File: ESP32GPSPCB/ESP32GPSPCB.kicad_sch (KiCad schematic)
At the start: 66 parts, among them J1 Conn_01x04_Socket, J2 USB_C_Receptacle_USB2.0_14P, J3 Conn_01x14_Socket, J4 Conn_01x04_Socket, J5 Boot Option, J6 Conn_01x04_Socket, J7 Conn_01x05_Socket, J8 Logic extra channel, SW1 SW_Push, U1 NEO-M8N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

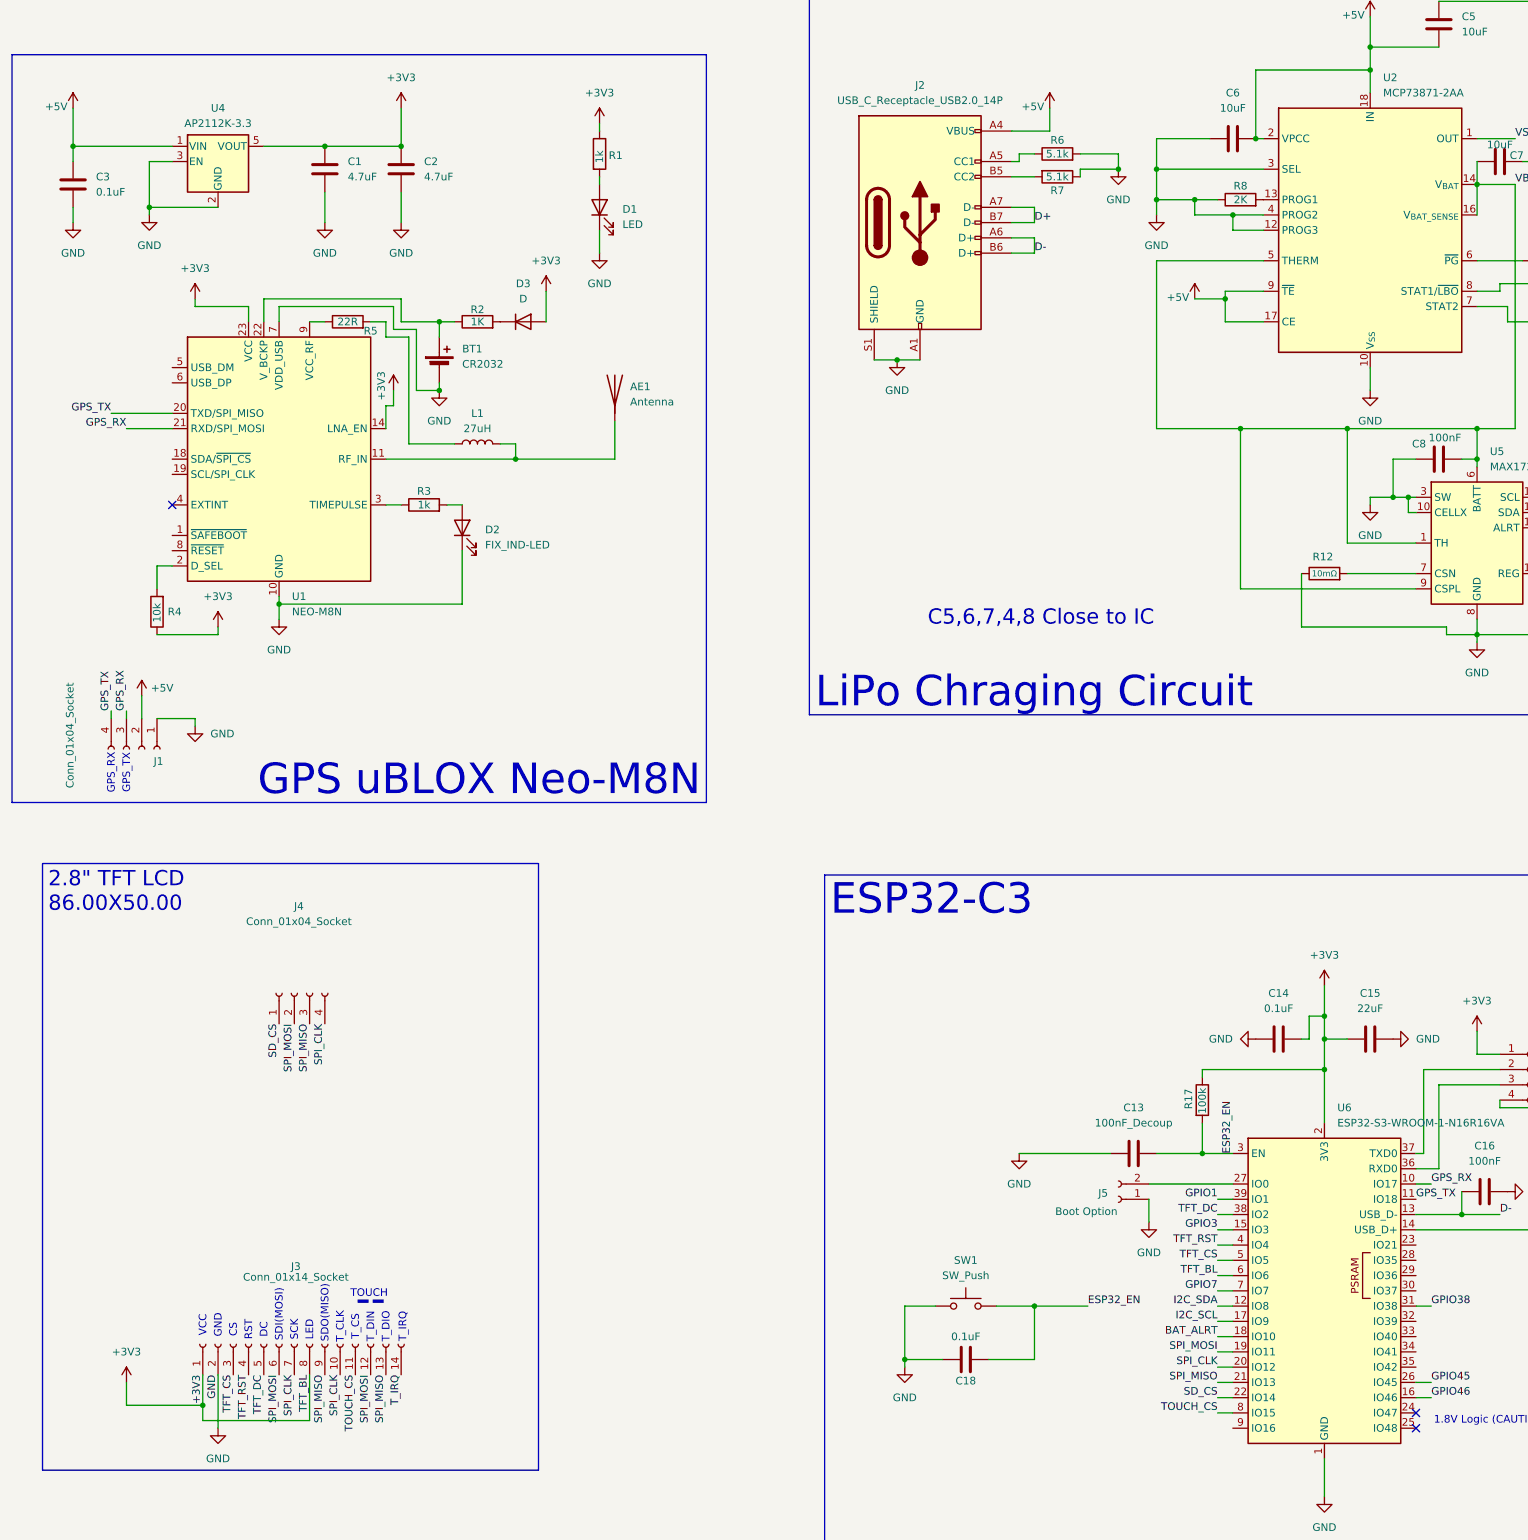
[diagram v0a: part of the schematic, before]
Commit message: schematic added, IMU finished, ERC RAN ERRORS FIXED
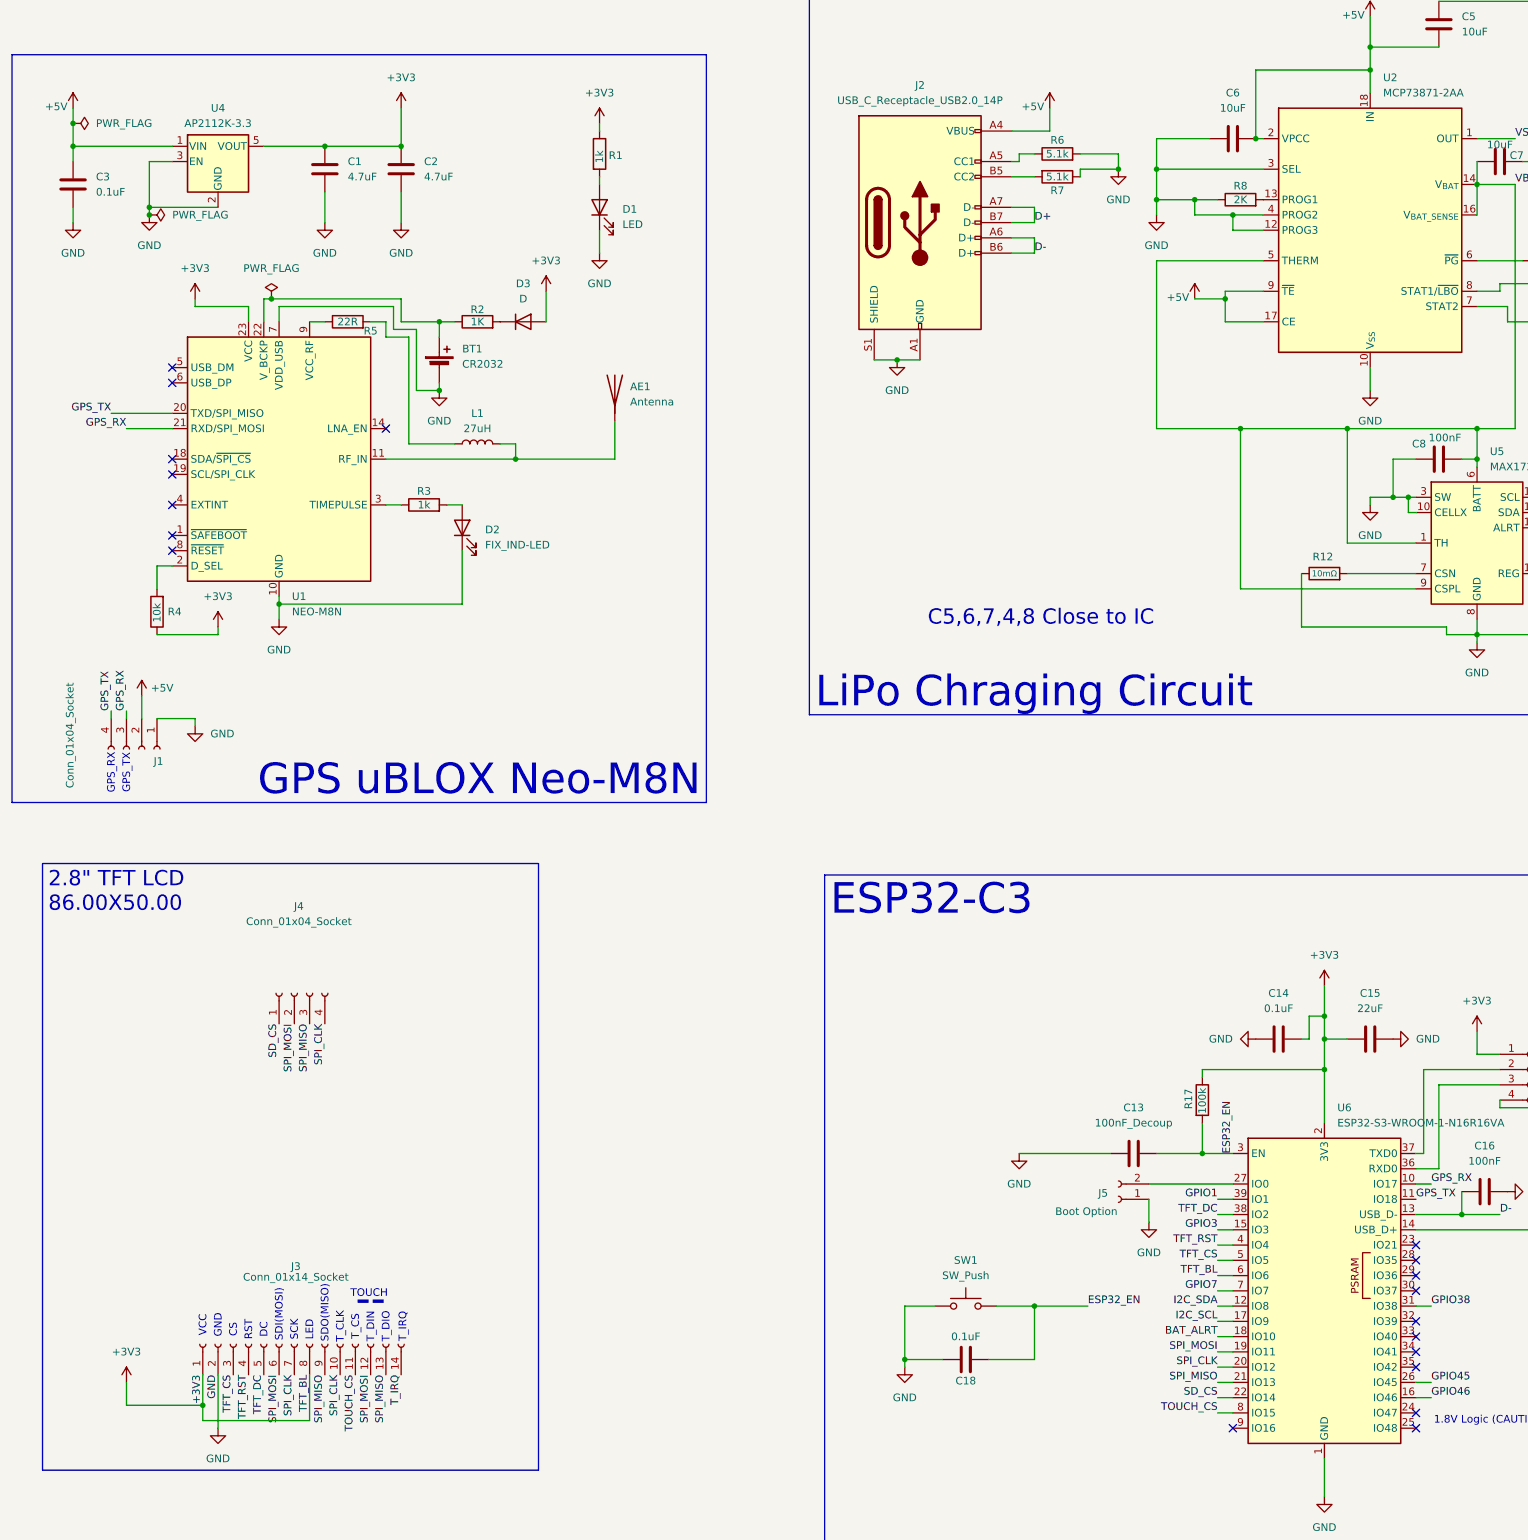
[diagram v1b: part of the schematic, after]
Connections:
- net +3V3: no longer U1.14 (LNA_EN)
- no-connect marks 5 -> 21
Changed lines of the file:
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@@
 	)
 	(junction
+		(at 66.04 77.47)
+		(diameter 0)
+		(color 0 0 0 0)
+	)
+	(junction
 		(at 480.06 82.55)
 		(diameter 0)
@@
 	)
 	(junction
+		(at 78.74 92.71)
+		(diameter 0)
+		(color 0 0 0 0)
+	)
+	(junction
+		(at 99.06 106.68)
+		(diameter 0)
+		(color 0 0 0 0)
+	)
+	(junction
 		(at 278.13 128.27)
 		(diameter 0)
@@
 	)
 	(no_connect
+		(at 82.55 133.35)
+	)
+	(no_connect
+		(at 82.55 118.11)
+	)
+	(no_connect
+		(at 289.56 281.94)
+	)
+	(no_connect
+		(at 118.11 128.27)
+	)
+	(no_connect
 		(at 289.56 292.1)
 	)
 	(no_connect
+		(at 82.55 120.65)
+	)
+	(no_connect
+		(at 289.56 266.7)
+	)
+	(no_connect
+		(at 289.56 276.86)
+	)
+	(no_connect
+		(at 82.55 135.89)
+	)
+	(no_connect
+		(at 289.56 284.48)
+	)
+	(no_connect
+		(at 82.55 148.59)
+	)
+	(no_connect
 		(at 497.84 259.08)
 	)
 	(no_connect
+		(at 82.55 146.05)
+	)
+	(no_connect
+		(at 289.56 269.24)
+	)
+	(no_connect
+		(at 289.56 279.4)
+	)
+	(no_connect
+		(at 259.08 294.64)
+	)
+	(no_connect
 		(at 82.55 140.97)
 	)
@@
 	)
 	(no_connect
+		(at 289.56 264.16)
+	)
+	(no_connect
+		(at 289.56 271.78)
+	)
+	(no_connect
 		(at 497.84 256.54)
 	)
@@
 	(wire
 		(pts
-			(xy 312.42 257.81) (xy 312.42 261.62)
+			(xy 66.04 77.47) (xy 66.04 81.28)
 		)
 		(stroke
@@
 	(wire
 		(pts
-			(xy 119.38 124.46) (xy 118.11 124.46)
+			(xy 312.42 257.81) (xy 312.42 261.62)
 		)
 		(stroke
@@
 	(wire
 		(pts
-			(xy 119.38 121.92) (xy 119.38 124.46)
-		)
-		(stroke
-			(width 0)
-			(type default)
-		)
-	)
-	(wire
-		(pts
 			(xy 74.93 290.83) (xy 74.93 287.02)
 		)
@@
 	(wire
 		(pts
-			(xy 118.11 124.46) (xy 118.11 128.27)
-		)
-		(stroke
-			(width 0)
-			(type default)
-		)
-	)
-	(wire
-		(pts
 			(xy 153.67 86.36) (xy 153.67 87.63)
 		)
@@
 	(wire
 		(pts
-			(xy 66.04 74.93) (xy 66.04 81.28)
+			(xy 66.04 74.93) (xy 66.04 77.47)
 		)
 		(stroke
@@
 	(wire
 		(pts
+			(xy 99.06 106.68) (xy 120.65 106.68)
+		)
+		(stroke
+			(width 0)
+			(type default)
+		)
+	)
+	(wire
+		(pts
 			(xy 82.55 151.13) (xy 80.01 151.13)
 		)
@@
 	(wire
 		(pts
-			(xy 97.79 106.68) (xy 120.65 106.68)
+			(xy 97.79 106.68) (xy 99.06 106.68)
 		)
 		(stroke
@@
 	)
 	(symbol
+		(lib_id "power:PWR_FLAG")
+		(at 99.06 106.68 0)
+		(unit 1)
+		(exclude_from_sim no)
+		(in_bom yes)
+		(on_board yes)
+		(dnp no)
+		(fields_autoplaced yes)
+		(property "Reference" "#FLG03"
+			(at 99.06 104.775 0)
+			(effects
+				(font
+					(size 1.27 1.27)
+				)
+				(hide yes)
+			)
+		)
+		(property "Value" "PWR_FLAG"
+			(at 99.06 101.6 0)
+			(effects
+				(font
+					(size 1.27 1.27)
+				)
+			)
+		)
+		(property "Footprint" ""
+			(at 99.06 106.68 0)
+			(effects
+				(font
+					(size 1.27 1.27)
+				)
+				(hide yes)
+			)
+		)
+		(property "Datasheet" "~"
+			(at 99.06 106.68 0)
+			(effects
+				(font
+					(size 1.27 1.27)
+				)
+				(hide yes)
+			)
+		)
+		(property "Description" "Special symbol for telling ERC where power comes from"
+			(at 99.06 106.68 0)
+			(effects
+				(font
+					(size 1.27 1.27)
+				)
+				(hide yes)
+			)
+		)
+		(pin "1"
+		)
+		(instances
+			(project "ESP32GPSPCB"
+				(path "/d0783557-2029-46ea-9a99-391ccdba8d69"
+					(reference "#FLG03")
+					(unit 1)
+				)
+			)
+		)
+	)
+	(symbol
 		(lib_id "power:GND")
 		(at 299.72 163.83 0)
@@
 	)
 	(symbol
-		(lib_id "power:+3V3")
-		(at 119.38 121.92 0)
-		(unit 1)
-		(exclude_from_sim no)
-		(in_bom yes)
-		(on_board yes)
-		(dnp no)
-		(property "Reference" "#PWR016"
-			(at 119.38 125.73 0)
-			(effects
-				(font
-					(size 1.27 1.27)
-				)
-				(hide yes)
-			)
-		)
-		(property "Value" "+3V3"
-			(at 117.348 121.158 90)
-			(effects
-				(font
-					(size 1.27 1.27)
-				)
-			)
-		)
-		(property "Footprint" ""
-			(at 119.38 121.92 0)
-			(effects
-				(font
-					(size 1.27 1.27)
-				)
-				(hide yes)
-			)
-		)
-		(property "Datasheet" ""
-			(at 119.38 121.92 0)
-			(effects
-				(font
-					(size 1.27 1.27)
-				)
-				(hide yes)
-			)
-		)
-		(property "Description" "Power symbol creates a global label with name \"+3V3\""
-			(at 119.38 121.92 0)
-			(effects
-				(font
-					(size 1.27 1.27)
-				)
-				(hide yes)
-			)
-		)
-		(pin "1"
-		)
-		(instances
-			(project "ESP32GPSPCB"
-				(path "/d0783557-2029-46ea-9a99-391ccdba8d69"
-					(reference "#PWR016")
-					(unit 1)
-				)
-			)
-		)
-	)
-	(symbol
 		(lib_id "power:GND")
 		(at 499.11 236.22 0)
@@
 	)
 	(symbol
+		(lib_id "power:PWR_FLAG")
+		(at 66.04 77.47 270)
+		(unit 1)
+		(exclude_from_sim no)
+		(in_bom yes)
+		(on_board yes)
+		(dnp no)
+		(fields_autoplaced yes)
+		(property "Reference" "#FLG01"
+			(at 67.945 77.47 0)
+			(effects
+				(font
+					(size 1.27 1.27)
+				)
+				(hide yes)
+			)
+		)
+		(property "Value" "PWR_FLAG"
+			(at 69.85 77.4699 90)
+			(effects
+				(font
+					(size 1.27 1.27)
+				)
+				(justify left)
+			)
+		)
+		(property "Footprint" ""
+			(at 66.04 77.47 0)
+			(effects
+				(font
+					(size 1.27 1.27)
+				)
+				(hide yes)
+			)
+		)
+		(property "Datasheet" "~"
+			(at 66.04 77.47 0)
+			(effects
+				(font
+					(size 1.27 1.27)
+				)
+				(hide yes)
+			)
+		)
+		(property "Description" "Special symbol for telling ERC where power comes from"
+			(at 66.04 77.47 0)
+			(effects
+				(font
+					(size 1.27 1.27)
+				)
+				(hide yes)
+			)
+		)
+		(pin "1"
+		)
+		(instances
+			(project ""
+				(path "/d0783557-2029-46ea-9a99-391ccdba8d69"
+					(reference "#FLG01")
+					(unit 1)
+				)
+			)
+		)
+	)
+	(symbol
 		(lib_id "power:GND")
 		(at 468.63 264.16 270)
@@
 					(unit 1)
 				)
+			)
+		)
+	)
+	(symbol
+		(lib_id "power:PWR_FLAG")
+		(at 78.74 92.71 270)
+		(unit 1)
+		(exclude_from_sim no)
+		(in_bom yes)
+		(on_board yes)
+		(dnp no)
+		(fields_autoplaced yes)
+		(property "Reference" "#FLG02"
+			(at 80.645 92.71 0)
+			(effects
+				(font
+					(size 1.27 1.27)
+				)
+				(hide yes)
+			)
+		)
+		(property "Value" "PWR_FLAG"
+			(at 82.55 92.7099 90)
+			(effects
+				(font
+					(size 1.27 1.27)
+				)
+				(justify left)
+			)
+		)
+		(property "Footprint" ""
+			(at 78.74 92.71 0)
+			(effects
+				(font
+					(size 1.27 1.27)
+				)
+				(hide yes)
+			)
+		)
+		(property "Datasheet" "~"
+			(at 78.74 92.71 0)
+			(effects
+				(font
+					(size 1.27 1.27)
+				)
+				(hide yes)
+			)
+		)
+		(property "Description" "Special symbol for telling ERC where power comes from"
+			(at 78.74 92.71 0)
+			(effects
+				(font
+					(size 1.27 1.27)
+				)
+				(hide yes)
+			)
+		)
+		(pin "1"
+		)
+		(instances
+			(project ""
+				(path "/d0783557-2029-46ea-9a99-391ccdba8d69"
+					(reference "#FLG02")
+					(unit 1)
+				)

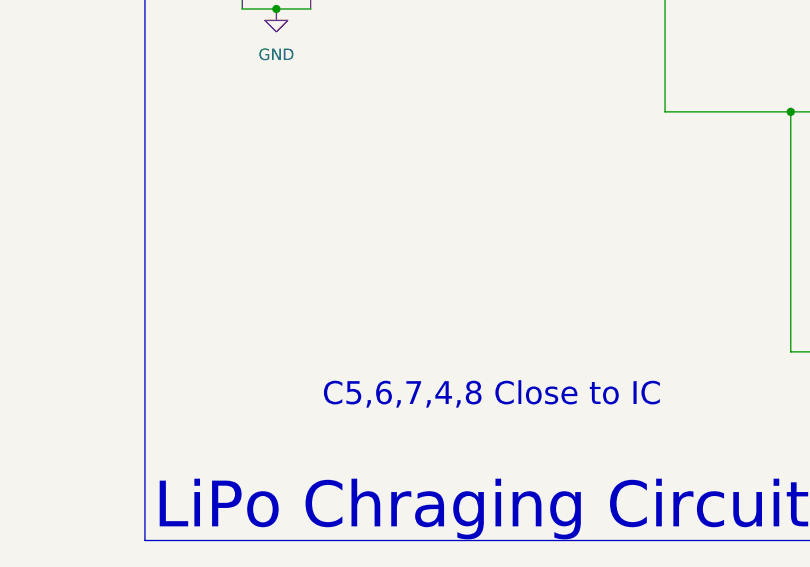
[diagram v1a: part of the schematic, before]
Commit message: placed all components
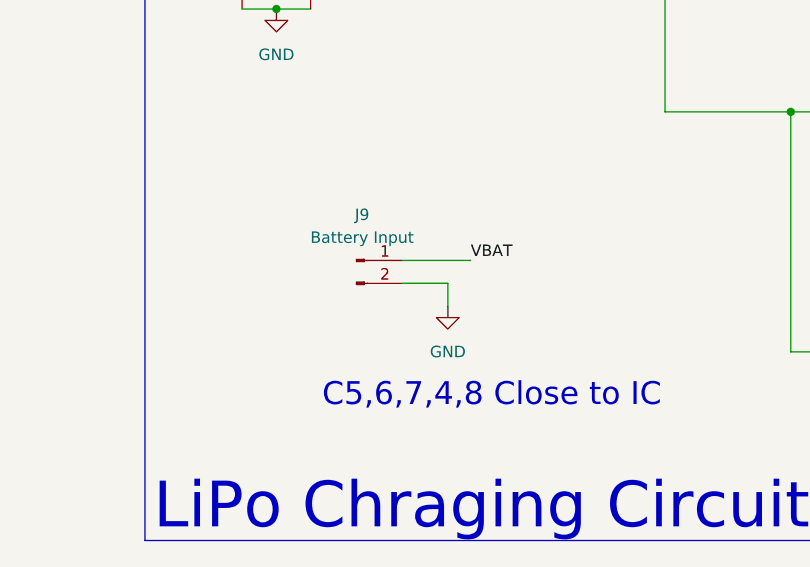
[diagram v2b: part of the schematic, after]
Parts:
- added J9: Battery Input, Connector_JST:JST_PH_B2B-PH-K_1x02_P2.00mm_Vertical, symbol Connector:Conn_01x02_Pin
- AE1: footprint (none) -> Connector_Coaxial:U.FL_Hirose_U.FL-R-SMT-1_Vertical
- BT1: footprint (none) -> Battery:BatteryHolder_Keystone_500
- C1, C10, C2, C3, C9: footprint (none) -> Capacitor_SMD:C_0805_2012Metric
- C11, C12, C14, C15, C16, C17, C19, C20, C4, C5, C6, C7, C8: footprint (none) -> Capacitor_SMD:C_0603_1608Metric
- C13, C18, C21, C22: footprint (none) -> Capacitor_SMD:C_0402_1005Metric
- D1: footprint (none) -> LED_SMD:LED_0402_1005Metric
- D2, D4, D5: footprint (none) -> LED_SMD:LED_0805_2012Metric
- D3: footprint (none) -> Diode_SMD:D_0603_1608Metric
- J1, J4, J6: footprint (none) -> Connector_PinHeader_2.54mm:PinHeader_1x04_P2.54mm_Vertical
- J2: footprint (none) -> Connector_USB:USB_C_Receptacle_HCTL_HC-TYPE-C-16P-01A
- J3: footprint (none) -> Connector_PinHeader_2.54mm:PinHeader_1x14_P2.54mm_Vertical
- J5, J8: footprint (none) -> Connector_PinHeader_2.54mm:PinHeader_1x02_P2.54mm_Vertical
- J7: footprint (none) -> Connector_PinHeader_2.54mm:PinHeader_1x05_P2.54mm_Vertical
- L1: footprint (none) -> Inductor_SMD:L_0603_1608Metric
- L2: footprint (none) -> Inductor_SMD:L_0402_1005Metric
- R1, R10, R11, R12, R13, R14, R15, R16, R2, R3, R4, R5, R6, R7, R8, R9: footprint (none) -> Resistor_SMD:R_0402_1005Metric
- R17: footprint (none) -> Resistor_SMD:R_0603_1608Metric
- SW1: footprint (none) -> Button_Switch_SMD:SW_Push_1P1T_NO_CK_KMR2
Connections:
- net GND: now also J9.2 (Pin_2)
- net VBAT: now also J9.1 (Pin_1)
